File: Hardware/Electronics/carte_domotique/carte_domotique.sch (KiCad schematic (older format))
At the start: 3 parts, among them J1 Conn_02x08_Counter_Clockwise, J2 Raspberry_Pi_2_3, J3 Conn_01x02

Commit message: motification du conneteur pour le raspbee II
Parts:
- removed J1: Conn_02x08_Counter_Clockwise, Connector_PinHeader_2.54mm:PinHeader_2x08_P2.54mm_Vertical, symbol Connector_Generic:Conn_02x08_Counter_Clockwise
- added J1: Conn_02x06_Odd_Even, Connector_PinHeader_2.54mm:PinHeader_2x06_P2.54mm_Vertical, symbol Connector_Generic:Conn_02x06_Odd_Even
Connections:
- wire segments 72 -> 53
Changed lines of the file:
@@
 $EndDescr
-$Comp
-L Connector_Generic:Conn_02x08_Counter_Clockwise J1
-U 1 1 61807EE4
-P 7600 2650
-F 0 "J1" H 7650 3167 50  0000 C CNN
-F 1 "Conn_02x08_Counter_Clockwise" H 7650 3076 50  0000 C CNN
-F 2 "Connector_PinHeader_2.54mm:PinHeader_2x08_P2.54mm_Vertical" H 7600 2650 50  0001 C CNN
-F 3 "~" H 7600 2650 50  0001 C CNN
-	1    7600 2650
-	1    0    0    -1
-$EndComp
 $Comp
 L Connector_Generic:Conn_01x02 J3
@@
 $EndComp
 Wire Wire Line
-	5800 4250 5700 4250
-Connection ~ 5800 4250
-Connection ~ 6400 4250
-Wire Wire Line
-	6400 4250 6300 4250
-Connection ~ 6300 4250
-Wire Wire Line
-	6300 4250 6200 4250
-Connection ~ 6200 4250
-Wire Wire Line
-	6200 4250 6100 4250
-Connection ~ 6100 4250
-Wire Wire Line
-	6100 4250 6000 4250
-Connection ~ 6000 4250
-Wire Wire Line
 	6000 1650 5950 1650
-Wire Wire Line
-	5900 1650 5300 1650
-Connection ~ 5900 1650
-Wire Wire Line
-	6000 4250 5900 4250
-Wire Wire Line
-	5900 4250 5800 4250
-Connection ~ 5900 4250
-$Comp
-L Connector:Raspberry_Pi_2_3 J2
-U 1 1 618062FD
-P 6100 2950
-F 0 "J2" H 6100 4431 50  0000 C CNN
-F 1 "Raspberry_Pi_2_3" H 6100 4340 50  0000 C CNN
-F 2 "Connector_PinSocket_2.54mm:PinSocket_2x20_P2.54mm_Vertical" H 6100 2950 50  0001 C CNN
-F 3 "https://www.raspberrypi.org/documentation/hardware/raspberrypi/schematics/rpi_SCH_3bplus_1p0_reduced.pdf" H 6100 2950 50  0001 C CNN
-	1    6100 2950
-	1    0    0    -1
-$EndComp
 Wire Wire Line
 	5950 1650 5950 1500
 Connection ~ 5950 1650
-Wire Wire Line
-	5950 1650 5900 1650
 Wire Wire Line
 	5950 1500 7400 1500
@@
 Wire Wire Line
 	7400 1500 7900 1500
-Wire Wire Line
-	7900 2450 7900 2350
-Connection ~ 7900 2350
 Wire Wire Line
 	7900 2550 8050 2550
@@
 	7200 1900 7200 1650
 Wire Wire Line
-	6200 1650 6300 1650
-Connection ~ 6300 1650
-Wire Wire Line
-	6300 1650 7200 1650
-Wire Wire Line
-	8250 4250 8250 2950
-Wire Wire Line
-	8250 1750 8050 1750
-Wire Wire Line
-	6400 4250 7050 4250
-Connection ~ 8050 1750
-Wire Wire Line
 	7400 2450 7150 2450
 Wire Wire Line
@@
 	7400 2650 6900 2650
 Wire Wire Line
-	7900 2350 7900 1850
-Wire Wire Line
 	7900 2650 8750 2650
 Wire Wire Line
@@
 Wire Wire Line
 	7050 2750 7050 4250
-Connection ~ 7050 4250
-Wire Wire Line
-	7050 4250 8250 4250
 Wire Wire Line
 	7900 2750 8800 2750
@@
 	5750 2450 5300 2450
 Wire Wire Line
-	5750 2850 7400 2850
-Wire Wire Line
 	7900 2850 8900 2850
 Wire Wire Line
@@
 	5000 1200 5000 2550
 Wire Wire Line
+	7900 1850 7900 2350
+$Comp
+L Connector_Generic:Conn_02x06_Odd_Even J1
+U 1 1 61835B69
+P 7600 2550
+F 0 "J1" H 7650 2967 50  0000 C CNN
+F 1 "Conn_02x06_Odd_Even" H 7650 2876 50  0000 C CNN
+F 2 "Connector_PinHeader_2.54mm:PinHeader_2x06_P2.54mm_Vertical" H 7600 2550 50  0001 C CNN
+F 3 "~" H 7600 2550 50  0001 C CNN
+	1    7600 2550
+	1    0    0    -1
+$EndComp
+Connection ~ 6300 1650
+Wire Wire Line
+	6300 1650 7200 1650
+Wire Wire Line
+	6200 1650 6300 1650
+Connection ~ 5900 4250
+Wire Wire Line
+	6000 4250 5900 4250
+Connection ~ 5900 1650
+Wire Wire Line
+	5950 1650 5900 1650
+Wire Wire Line
+	5900 1650 5300 1650
+Connection ~ 6000 4250
+Connection ~ 6100 4250
+Wire Wire Line
+	6100 4250 6000 4250
+Wire Wire Line
+	6200 4250 6100 4250
+Connection ~ 6200 4250
+Connection ~ 6300 4250
+Wire Wire Line
+	6300 4250 6200 4250
+Wire Wire Line
+	6400 4250 6300 4250
+Connection ~ 6400 4250
+Connection ~ 5800 4250
+Wire Wire Line
+	5900 4250 5800 4250
+Wire Wire Line
+	5800 4250 5700 4250
+Wire Wire Line
+	6400 4250 7050 4250
+Wire Wire Line
+	5750 2850 7400 2850
+Wire Wire Line
 	5000 2550 5300 2550
-Wire Wire Line
-	7400 2950 5550 2950
-Wire Wire Line
-	5550 2950 5550 3050
-Wire Wire Line
-	5550 3050 5150 3050
-Wire Wire Line
-	5150 3050 5150 3650
-Wire Wire Line
-	5150 3650 5300 3650
-Wire Wire Line
-	7900 2950 8250 2950
-Connection ~ 8250 2950
-Wire Wire Line
-	8250 2950 8250 1750
-Wire Wire Line
-	7400 3050 7400 3950
-Wire Wire Line
-	7400 3950 5800 3950
-Wire Wire Line
-	5800 3950 5800 3150
-Wire Wire Line
-	5800 3150 5300 3150
-Wire Wire Line
-	7900 3050 7900 4050
-Wire Wire Line
-	7900 4050 5700 4050
-Wire Wire Line
-	5700 4050 5700 3250
-Wire Wire Line
-	5700 3250 5300 3250
+$Comp
+L Connector:Raspberry_Pi_2_3 J2
+U 1 1 618062FD
+P 6100 2950
+F 0 "J2" H 6100 4431 50  0000 C CNN
+F 1 "Raspberry_Pi_2_3" H 6100 4340 50  0000 C CNN
+F 2 "Connector_PinSocket_2.54mm:PinSocket_2x20_P2.54mm_Vertical" H 6100 2950 50  0001 C CNN
+F 3 "https://www.raspberrypi.org/documentation/hardware/raspberrypi/schematics/rpi_SCH_3bplus_1p0_reduced.pdf" H 6100 2950 50  0001 C CNN
+	1    6100 2950
+	1    0    0    -1
+$EndComp
 $EndSCHEMATC

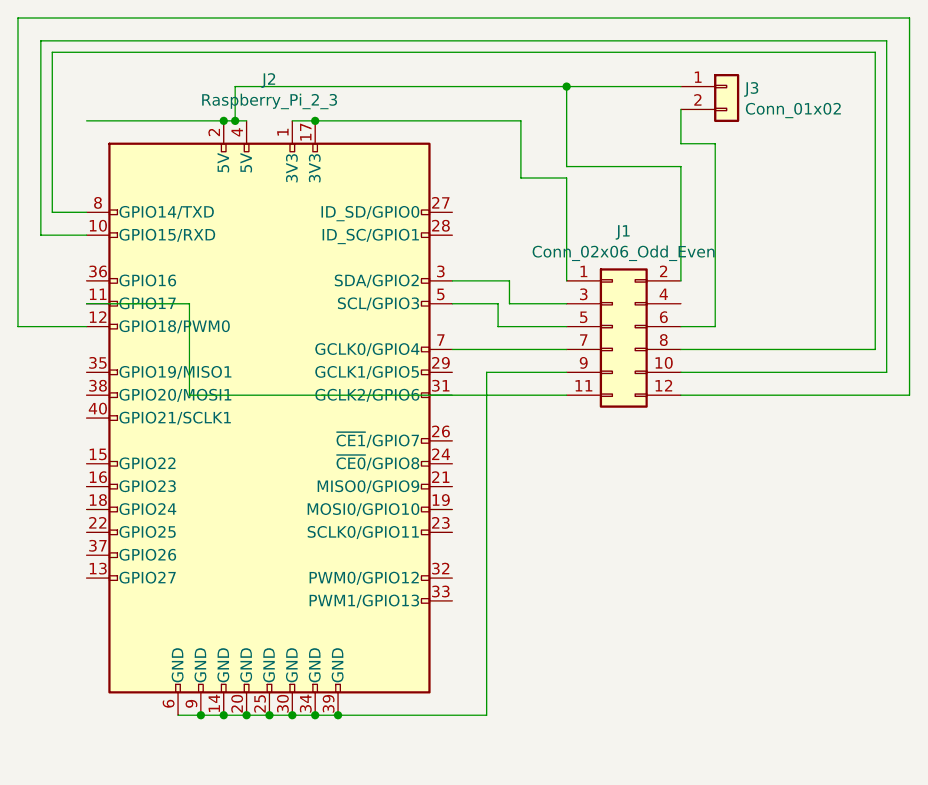
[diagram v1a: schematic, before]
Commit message: kicad+ doc
ajout de document
modification avec le cablage de l'antenne xbee d'après la datasheet
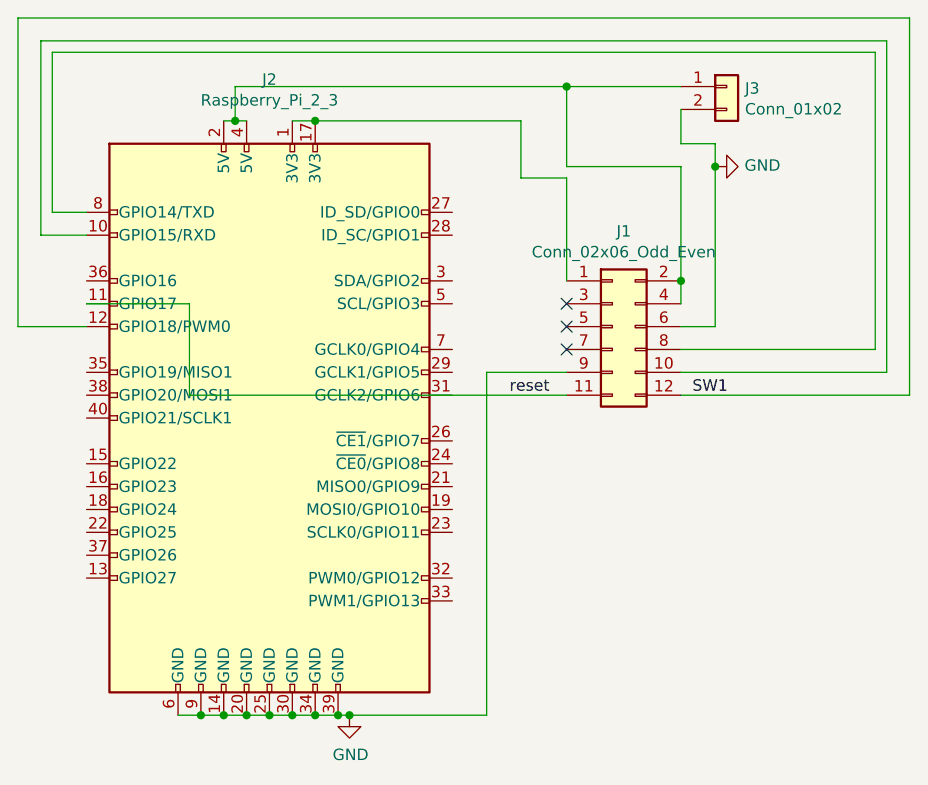
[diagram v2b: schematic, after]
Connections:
- net reset: now reaches J1.11 (Pin_11), J2.11 (GPIO17)
- net SW1: now reaches J1.12 (Pin_12), J2.12 (GPIO18/PWM0)
- net GND: now reaches J1.9 (Pin_9), J2.14 (GND), J2.20 (GND), J2.25 (GND), J2.30 (GND), J2.34 (GND), J2.39 (GND), J2.6 (GND), J2.9 (GND)
- net GND: now also J1.6 (Pin_6), J3.2 (Pin_2)
- net at J1.2 (Pin_2), J2.2 (5V), J2.4 (5V)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: now also J1.4 (Pin_4)
- net at J2.3 (SDA/GPIO2): no longer J1.3 (Pin_3)
- net at J2.5 (SCL/GPIO3): no longer J1.5 (Pin_5)
- net at J2.7 (GCLK0/GPIO4): no longer J1.7 (Pin_7)
- no-connect marks 0 -> 3
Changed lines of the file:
@@
 	7900 2550 8050 2550
 Wire Wire Line
-	8050 2550 8050 1750
+	8050 2550 8050 1850
 Wire Wire Line
 	8050 1750 7900 1750
@@
 Wire Wire Line
 	7200 1900 7200 1650
-Wire Wire Line
-	7400 2450 7150 2450
-Wire Wire Line
-	7150 2450 7150 2350
-Wire Wire Line
-	7150 2350 6900 2350
-Wire Wire Line
-	7400 2550 7100 2550
-Wire Wire Line
-	7100 2550 7100 2450
-Wire Wire Line
-	7100 2450 6900 2450
-Wire Wire Line
-	7400 2650 6900 2650
 Wire Wire Line
 	7900 2650 8750 2650
@@
 Wire Wire Line
 	5000 1200 5000 2550
-Wire Wire Line
-	7900 1850 7900 2350
 $Comp
 L Connector_Generic:Conn_02x06_Odd_Even J1
@@
 Wire Wire Line
 	6000 4250 5900 4250
-Connection ~ 5900 1650
 Wire Wire Line
 	5950 1650 5900 1650
-Wire Wire Line
-	5900 1650 5300 1650
 Connection ~ 6000 4250
 Connection ~ 6100 4250
@@
 	5800 4250 5700 4250
 Wire Wire Line
-	6400 4250 7050 4250
+	6400 4250 6450 4250
 Wire Wire Line
 	5750 2850 7400 2850
@@
 	1    0    0    -1
 $EndComp
+Wire Wire Line
+	7900 1850 7900 2350
+Connection ~ 7900 2350
+Wire Wire Line
+	7900 2350 7900 2450
+Text Label 7150 2850 0    50   ~ 0
+reset
+NoConn ~ 7400 2450
+NoConn ~ 7400 2550
+$Comp
+L power:GND #PWR?
+U 1 1 6184D882
+P 8050 1850
+F 0 "#PWR?" H 8050 1600 50  0001 C CNN
+F 1 "GND" V 8055 1722 50  0000 R CNN
+F 2 "" H 8050 1850 50  0001 C CNN
+F 3 "" H 8050 1850 50  0001 C CNN
+	1    8050 1850
+	0    -1   -1   0
+$EndComp
+Connection ~ 8050 1850
+Wire Wire Line
+	8050 1850 8050 1750
+$Comp
+L power:GND #PWR?
+U 1 1 6184DD94
+P 6450 4250
+F 0 "#PWR?" H 6450 4000 50  0001 C CNN
+F 1 "GND" H 6455 4077 50  0000 C CNN
+F 2 "" H 6450 4250 50  0001 C CNN
+F 3 "" H 6450 4250 50  0001 C CNN
+	1    6450 4250
+	1    0    0    -1
+$EndComp
+Connection ~ 6450 4250
+Wire Wire Line
+	6450 4250 7050 4250
+Text Label 7950 2850 0    50   ~ 0
+SW1
+NoConn ~ 7400 2650
 $EndSCHEMATC

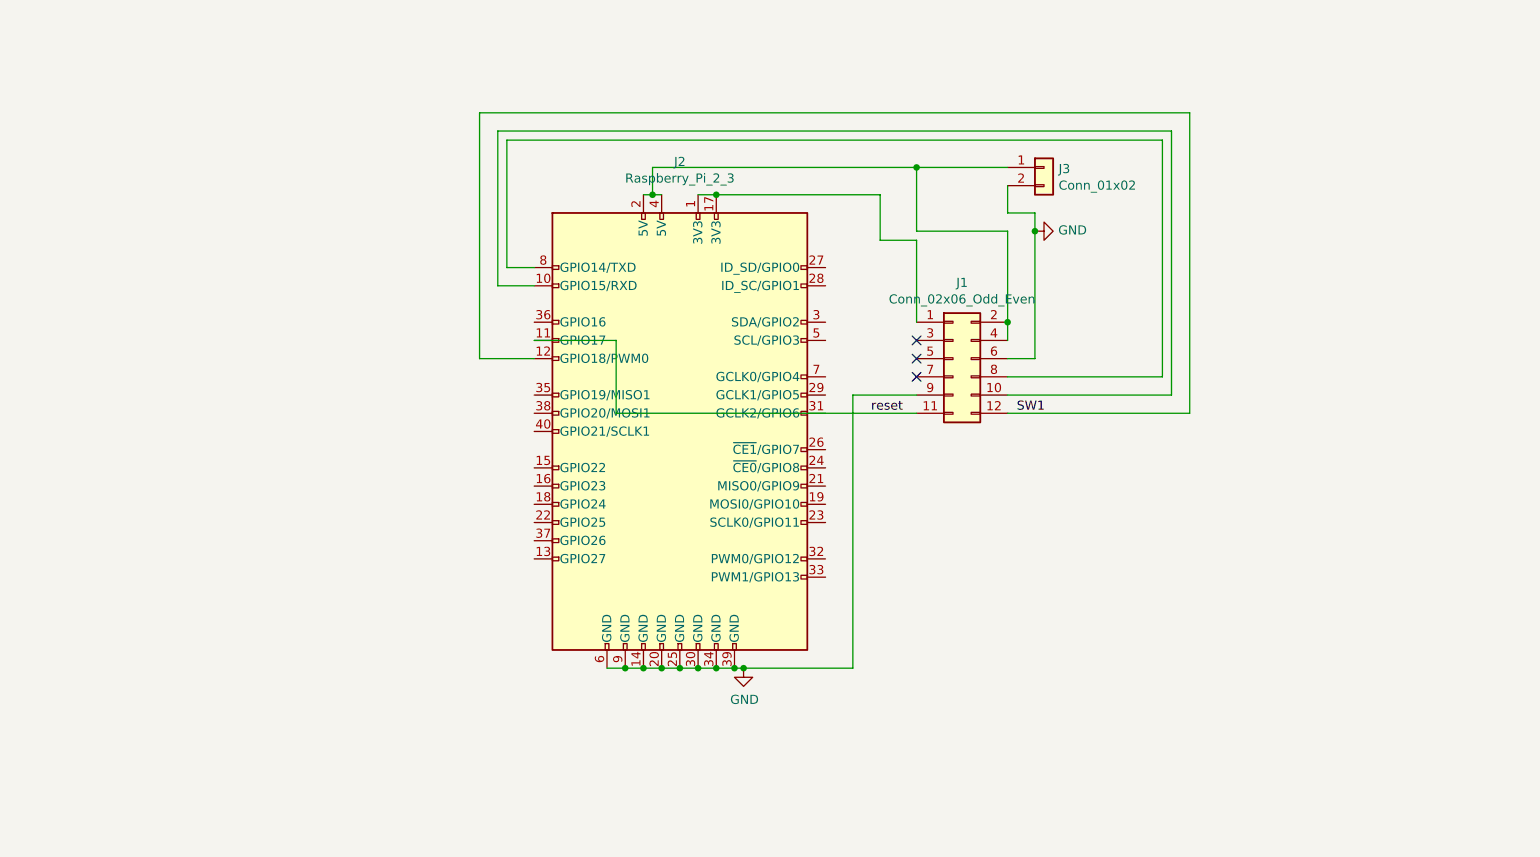
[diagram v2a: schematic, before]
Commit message: kicad
schematic + empreinte
tracage des bus
+ mise en place des connecteur spi i2c pwm pcm 5v 33v gnd
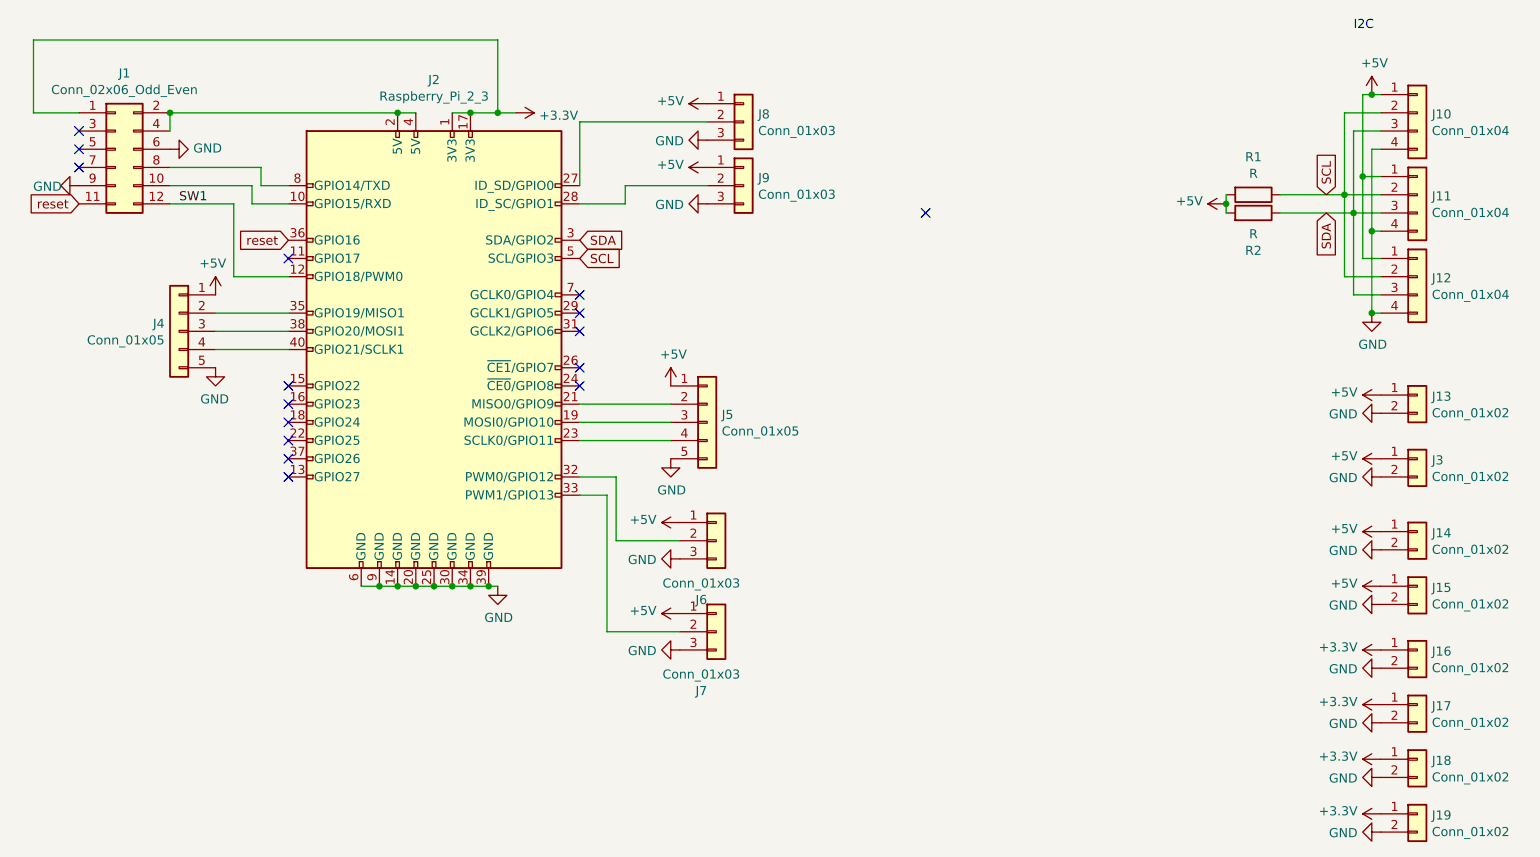
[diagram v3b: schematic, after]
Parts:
- added J10, J11, J12: Conn_01x04, Connector_PinHeader_2.54mm:PinHeader_1x04_P2.54mm_Vertical, symbol Connector_Generic:Conn_01x04
- added J13, J14, J15, J16, J17, J18, J19: Conn_01x02, Connector_PinHeader_2.54mm:PinHeader_1x02_P2.54mm_Vertical, symbol Connector_Generic:Conn_01x02
- added J4, J5: Conn_01x05, Connector_PinHeader_2.54mm:PinHeader_1x05_P2.54mm_Vertical, symbol Connector_Generic:Conn_01x05
- added J6, J7, J8, J9: Conn_01x03, Connector_PinHeader_2.54mm:PinHeader_1x03_P2.54mm_Vertical, symbol Connector_Generic:Conn_01x03
- added R1, R2: R, Resistor_SMD:R_1206_3216Metric_Pad1.42x1.75mm_HandSolder, symbol Device:R
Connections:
- net GND: now also J10.4 (Pin_4), J11.4 (Pin_4), J12.4 (Pin_4), J13.2 (Pin_2), J14.2 (Pin_2), J15.2 (Pin_2), J16.2 (Pin_2), J17.2 (Pin_2), J18.2 (Pin_2), J19.2 (Pin_2), J4.5 (Pin_5), J5.5 (Pin_5), J6.3 (Pin_3), J7.3 (Pin_3), J8.3 (Pin_3), J9.3 (Pin_3)
- net reset: now also J2.36 (GPIO16); no longer J2.11 (GPIO17)
- net +3V3: now reaches J1.1 (Pin_1), J2.1 (3V3), J2.17 (3V3)
- net +3V3: now also J16.1 (Pin_1), J17.1 (Pin_1), J18.1 (Pin_1), J19.1 (Pin_1)
- net at J2.19 (MOSI0/GPIO10): now also J5.3 (Pin_3)
- net at J1.2 (Pin_2), J1.4 (Pin_4), J2.2 (5V)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: no longer J3.1 (Pin_1)
- net at J2.21 (MISO0/GPIO9): now also J5.2 (Pin_2)
- net at J2.23 (SCLK0/GPIO11): now also J5.4 (Pin_4)
- net at J2.27 (ID_SD/GPIO0): now also J8.2 (Pin_2)
- net at J2.28 (ID_SC/GPIO1): now also J9.2 (Pin_2)
- net SDA: now reaches J2.3 (SDA/GPIO2)
- net SDA: now also J10.3 (Pin_3), J11.3 (Pin_3), J12.3 (Pin_3), R2.1
- net at J2.32 (PWM0/GPIO12): now also J6.2 (Pin_2)
- net at J2.33 (PWM1/GPIO13): now also J7.2 (Pin_2)
- net at J2.35 (GPIO19/MISO1): now also J4.2 (Pin_2)
- net at J2.38 (GPIO20/MOSI1): now also J4.3 (Pin_3)
- net at J2.40 (GPIO21/SCLK1): now also J4.4 (Pin_4)
- net SCL: now reaches J2.5 (SCL/GPIO3)
- net SCL: now also J10.2 (Pin_2), J11.2 (Pin_2), J12.2 (Pin_2), R1.1
- new net +5V: J10.1 (Pin_1), J11.1 (Pin_1), J12.1 (Pin_1), J13.1 (Pin_1), J14.1 (Pin_1), J15.1 (Pin_1), J3.1 (Pin_1), J4.1 (Pin_1), J5.1 (Pin_1), J6.1 (Pin_1), J7.1 (Pin_1), J8.1 (Pin_1), J9.1 (Pin_1), R1.2, R2.2
- no-connect marks 3 -> 16
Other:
- note added: "I2C"
- moved on the sheet: J1, J2, J3

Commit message: carte 1
carte proto 1
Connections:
- net +5V: now also J1.2 (Pin_2), J1.4 (Pin_4), J2.2 (5V), J2.4 (5V)
- net reset: now also J2.11 (GPIO17); no longer J2.36 (GPIO16)
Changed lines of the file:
@@
 	1    0    0    -1
 $EndComp
-Wire Wire Line
-	3650 2100 3950 2100
 $Comp
 L power:GND #PWR0101
@@
 Text GLabel 5550 1900 2    50   Input ~ 0
 SDA
-Text GLabel 3950 1900 0    50   Input ~ 0
-reset
 $Comp
 L Connector_Generic:Conn_01x02 J13
@@
 $EndComp
 Wire Wire Line
-	3750 1700 3950 1700
-Wire Wire Line
 	3300 1700 3650 1700
 Wire Wire Line
-	3650 1700 3650 2100
-Wire Wire Line
 	3300 1600 3750 1600
 Wire Wire Line
@@
 Wire Wire Line
 	3800 1500 3800 1600
-Connection ~ 4550 3800
-Connection ~ 4950 1200
-Wire Wire Line
-	4850 1200 4950 1200
-Wire Wire Line
-	4950 1200 5100 1200
-Connection ~ 4650 3800
-Wire Wire Line
-	4650 3800 4550 3800
-Wire Wire Line
-	4750 3800 4650 3800
-Connection ~ 4750 3800
-Connection ~ 4850 3800
-Wire Wire Line
-	4850 3800 4750 3800
-Wire Wire Line
-	4950 3800 4850 3800
-Connection ~ 4950 3800
-Connection ~ 5050 3800
-Wire Wire Line
-	5050 3800 4950 3800
-Wire Wire Line
-	5050 3800 5100 3800
-Connection ~ 4450 3800
-Wire Wire Line
-	4550 3800 4450 3800
-Wire Wire Line
-	4450 3800 4350 3800
-Wire Wire Line
-	5550 3000 6050 3000
-Wire Wire Line
-	5550 2900 6050 2900
-Wire Wire Line
-	5550 2800 6050 2800
-$Comp
-L Connector:Raspberry_Pi_2_3 J2
-U 1 1 618062FD
-P 4750 2500
-F 0 "J2" H 4750 3981 50  0000 C CNN
-F 1 "Raspberry_Pi_2_3" H 4750 3890 50  0000 C CNN
-F 2 "Connector_PinSocket_2.54mm:PinSocket_2x20_P2.54mm_Vertical" H 4750 2500 50  0001 C CNN
-F 3 "https://www.raspberrypi.org/documentation/hardware/raspberrypi/schematics/rpi_SCH_3bplus_1p0_reduced.pdf" H 4750 2500 50  0001 C CNN
-	1    4750 2500
-	1    0    0    -1
-$EndComp
 $Comp
 L power:GND #PWR0111
@@
 Wire Wire Line
 	3300 1300 3300 1200
-Wire Wire Line
-	3300 1200 4550 1200
 Connection ~ 3300 1200
-Connection ~ 4550 1200
 $Comp
 L Connector_Generic:Conn_01x02 J3
@@
 $EndComp
 Wire Wire Line
-	4550 1200 4650 1200
-Wire Wire Line
 	5100 1200 5100 800
 Wire Wire Line
@@
 	5550 1250 6250 1250
 Wire Wire Line
-	5550 1700 5800 1700
-Wire Wire Line
 	5800 1700 5800 1600
 Wire Wire Line
@@
 $EndComp
 Wire Wire Line
-	5550 3200 5750 3200
-Wire Wire Line
 	5750 3200 5750 3550
 Wire Wire Line
 	5750 3550 6100 3550
-Wire Wire Line
-	5550 3300 5700 3300
 Wire Wire Line
 	5700 3300 5700 4050
@@
 Wire Wire Line
 	5700 4050 6100 4050
-NoConn ~ 3950 2000
 NoConn ~ 5550 2200
 NoConn ~ 5550 2300
@@
 NoConn ~ 3950 3200
 NoConn ~ 7450 1750
+Connection ~ 4550 1200
+Wire Wire Line
+	3300 1200 3950 1200
+Connection ~ 4450 3800
+Wire Wire Line
+	5050 3800 5100 3800
+Connection ~ 5050 3800
+Connection ~ 4950 3800
+Connection ~ 4850 3800
+Connection ~ 4750 3800
+Connection ~ 4650 3800
+Connection ~ 4950 1200
+Connection ~ 4550 3800
+Wire Wire Line
+	5550 3300 5700 3300
+Wire Wire Line
+	5550 3200 5750 3200
+Wire Wire Line
+	5550 3000 6050 3000
+Wire Wire Line
+	5550 2900 6050 2900
+Wire Wire Line
+	5550 2800 6050 2800
+Wire Wire Line
+	5550 1700 5800 1700
+Wire Wire Line
+	5050 3800 4950 3800
+Wire Wire Line
+	4950 1200 5100 1200
+Wire Wire Line
+	4950 3800 4850 3800
+Wire Wire Line
+	4850 1200 4950 1200
+Wire Wire Line
+	4850 3800 4750 3800
+Wire Wire Line
+	4750 3800 4650 3800
+Wire Wire Line
+	4650 3800 4550 3800
+Wire Wire Line
+	4550 1200 4650 1200
+Wire Wire Line
+	4550 3800 4450 3800
+Wire Wire Line
+	4450 3800 4350 3800
+NoConn ~ 3950 1900
+$Comp
+L Connector:Raspberry_Pi_2_3 J2
+U 1 1 618062FD
+P 4750 2500
+F 0 "J2" H 4750 3981 50  0000 C CNN
+F 1 "Raspberry_Pi_2_3" H 4750 3890 50  0000 C CNN
+F 2 "Connector_PinSocket_2.54mm:PinSocket_2x20_P2.54mm_Vertical" H 4750 2500 50  0001 C CNN
+F 3 "https://www.raspberrypi.org/documentation/hardware/raspberrypi/schematics/rpi_SCH_3bplus_1p0_reduced.pdf" H 4750 2500 50  0001 C CNN
+	1    4750 2500
+	1    0    0    -1
+$EndComp
+Wire Wire Line
+	3650 2100 3950 2100
+Wire Wire Line
+	3750 1700 3950 1700
+Wire Wire Line
+	3650 1700 3650 2100
+Text GLabel 3950 2000 0    50   Input ~ 0
+reset
+$Comp
+L power:+5V #PWR?
+U 1 1 61C061AB
+P 3950 1200
+F 0 "#PWR?" H 3950 1050 50  0001 C CNN
+F 1 "+5V" H 3965 1328 50  0000 L CNN
+F 2 "" H 3950 1200 50  0001 C CNN
+F 3 "" H 3950 1200 50  0001 C CNN
+	1    3950 1200
+	1    0    0    -1
+$EndComp
+Connection ~ 3950 1200
+Wire Wire Line
+	3950 1200 4550 1200
 $EndSCHEMATC
